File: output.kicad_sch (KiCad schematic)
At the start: 12 parts, among them Q1 DMN6075S, Q2 DMN6075S, Q3 DMN6075S, Q4 DMN6075S

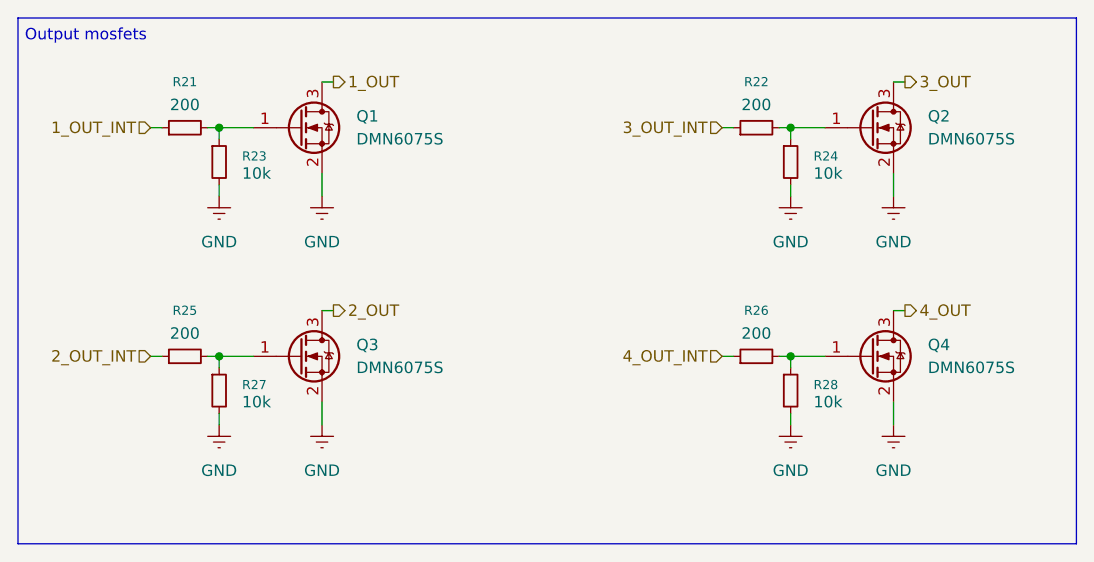
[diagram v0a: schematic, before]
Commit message: change voltage regulators
change can transciever
add more useful parts to can setup
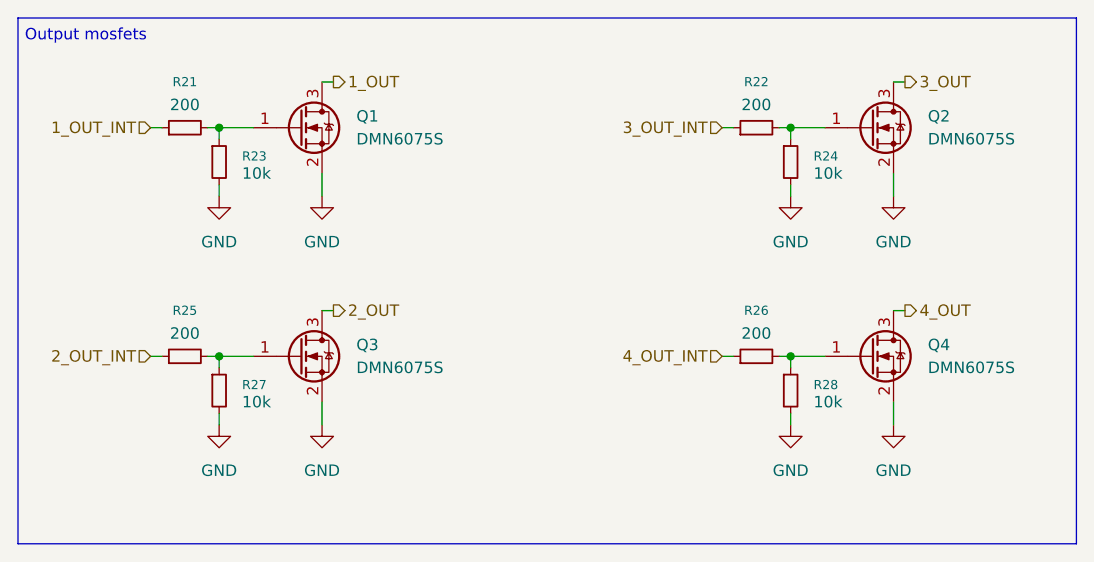
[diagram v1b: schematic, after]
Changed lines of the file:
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@@
 	)
 	(symbol
-		(lib_id "power:GNDREF")
+		(lib_id "power:GND")
 		(at 114.3 96.52 0)
 		(unit 1)
@@
 			)
 		)
-		(property "Description" "Power symbol creates a global label with name \"GNDREF\" , reference supply ground"
+		(property "Description" "Power symbol creates a global label with name \"GND\" , ground"
 			(at 114.3 96.52 0)
 			(effects
@@
 	)
 	(symbol
-		(lib_id "power:GNDREF")
+		(lib_id "power:GND")
 		(at 114.3 121.92 0)
 		(unit 1)
@@
 			)
 		)
-		(property "Description" "Power symbol creates a global label with name \"GNDREF\" , reference supply ground"
+		(property "Description" "Power symbol creates a global label with name \"GND\" , ground"
 			(at 114.3 121.92 0)
 			(effects
@@
 	)
 	(symbol
-		(lib_id "power:GNDREF")
+		(lib_id "power:GND")
 		(at 189.23 121.92 0)
 		(unit 1)
@@
 			)
 		)
-		(property "Description" "Power symbol creates a global label with name \"GNDREF\" , reference supply ground"
+		(property "Description" "Power symbol creates a global label with name \"GND\" , ground"
 			(at 189.23 121.92 0)
 			(effects
@@
 	)
 	(symbol
-		(lib_id "power:GNDREF")
+		(lib_id "power:GND")
 		(at 125.73 121.92 0)
 		(unit 1)
@@
 			)
 		)
-		(property "Description" "Power symbol creates a global label with name \"GNDREF\" , reference supply ground"
+		(property "Description" "Power symbol creates a global label with name \"GND\" , ground"
 			(at 125.73 121.92 0)
 			(effects
@@
 	)
 	(symbol
-		(lib_id "power:GNDREF")
+		(lib_id "power:GND")
 		(at 177.8 121.92 0)
 		(unit 1)
@@
 			)
 		)
-		(property "Description" "Power symbol creates a global label with name \"GNDREF\" , reference supply ground"
+		(property "Description" "Power symbol creates a global label with name \"GND\" , ground"
 			(at 177.8 121.92 0)
 			(effects
@@
 	)
 	(symbol
-		(lib_id "power:GNDREF")
+		(lib_id "power:GND")
 		(at 189.23 96.52 0)
 		(unit 1)
@@
 			)
 		)
-		(property "Description" "Power symbol creates a global label with name \"GNDREF\" , reference supply ground"
+		(property "Description" "Power symbol creates a global label with name \"GND\" , ground"
 			(at 189.23 96.52 0)
 			(effects
@@
 	)
 	(symbol
-		(lib_id "power:GNDREF")
+		(lib_id "power:GND")
 		(at 177.8 96.52 0)
 		(unit 1)
@@
 			)
 		)
-		(property "Description" "Power symbol creates a global label with name \"GNDREF\" , reference supply ground"
+		(property "Description" "Power symbol creates a global label with name \"GND\" , ground"
 			(at 177.8 96.52 0)
 			(effects
@@
 	)
 	(symbol
-		(lib_id "power:GNDREF")
+		(lib_id "power:GND")
 		(at 125.73 96.52 0)
 		(unit 1)
@@
 			)
 		)
-		(property "Description" "Power symbol creates a global label with name \"GNDREF\" , reference supply ground"
+		(property "Description" "Power symbol creates a global label with name \"GND\" , ground"
 			(at 125.73 96.52 0)
 			(effects

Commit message: group parts on pcb
replace footprints
update can setup
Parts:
- R21, R22, R23, R24, R25, R26, R27, R28: footprint (none) -> Resistor_SMD:R_0603_1608Metric
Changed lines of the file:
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@@
 			)
 		)
-		(property "Footprint" ""
+		(property "Footprint" "Resistor_SMD:R_0603_1608Metric"
 			(at 114.3 92.71 0)
 			(effects
@@
 			)
 		)
-		(property "Footprint" ""
+		(property "Footprint" "Resistor_SMD:R_0603_1608Metric"
 			(at 114.3 118.11 0)
 			(effects
@@
 			)
 		)
-		(property "Footprint" ""
+		(property "Footprint" "Resistor_SMD:R_0603_1608Metric"
 			(at 110.49 114.3 0)
 			(effects
@@
 			)
 		)
-		(property "Footprint" ""
+		(property "Footprint" "Resistor_SMD:R_0603_1608Metric"
 			(at 173.99 114.3 0)
 			(effects
@@
 			)
 		)
-		(property "Footprint" ""
+		(property "Footprint" "Resistor_SMD:R_0603_1608Metric"
 			(at 173.99 88.9 0)
 			(effects
@@
 			)
 		)
-		(property "Footprint" ""
+		(property "Footprint" "Resistor_SMD:R_0603_1608Metric"
 			(at 110.49 88.9 0)
 			(effects
@@
 			)
 		)
-		(property "Footprint" ""
+		(property "Footprint" "Resistor_SMD:R_0603_1608Metric"
 			(at 177.8 92.71 0)
 			(effects
@@
 			)
 		)
-		(property "Footprint" ""
+		(property "Footprint" "Resistor_SMD:R_0603_1608Metric"
 			(at 177.8 118.11 0)
 			(effects
